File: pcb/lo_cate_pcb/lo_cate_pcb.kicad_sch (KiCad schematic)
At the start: 42 parts, among them J1 Conn_01x07_Pin, J2 690-005-299-043, SW1 MICRO_RESET, SW2 MICRO_ON, SW3 BUTTON1, SW4 BUTTON2, SW5 BUTTON3, U1 STM32F401RETx, U2 BMI323, U3 150141M173100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

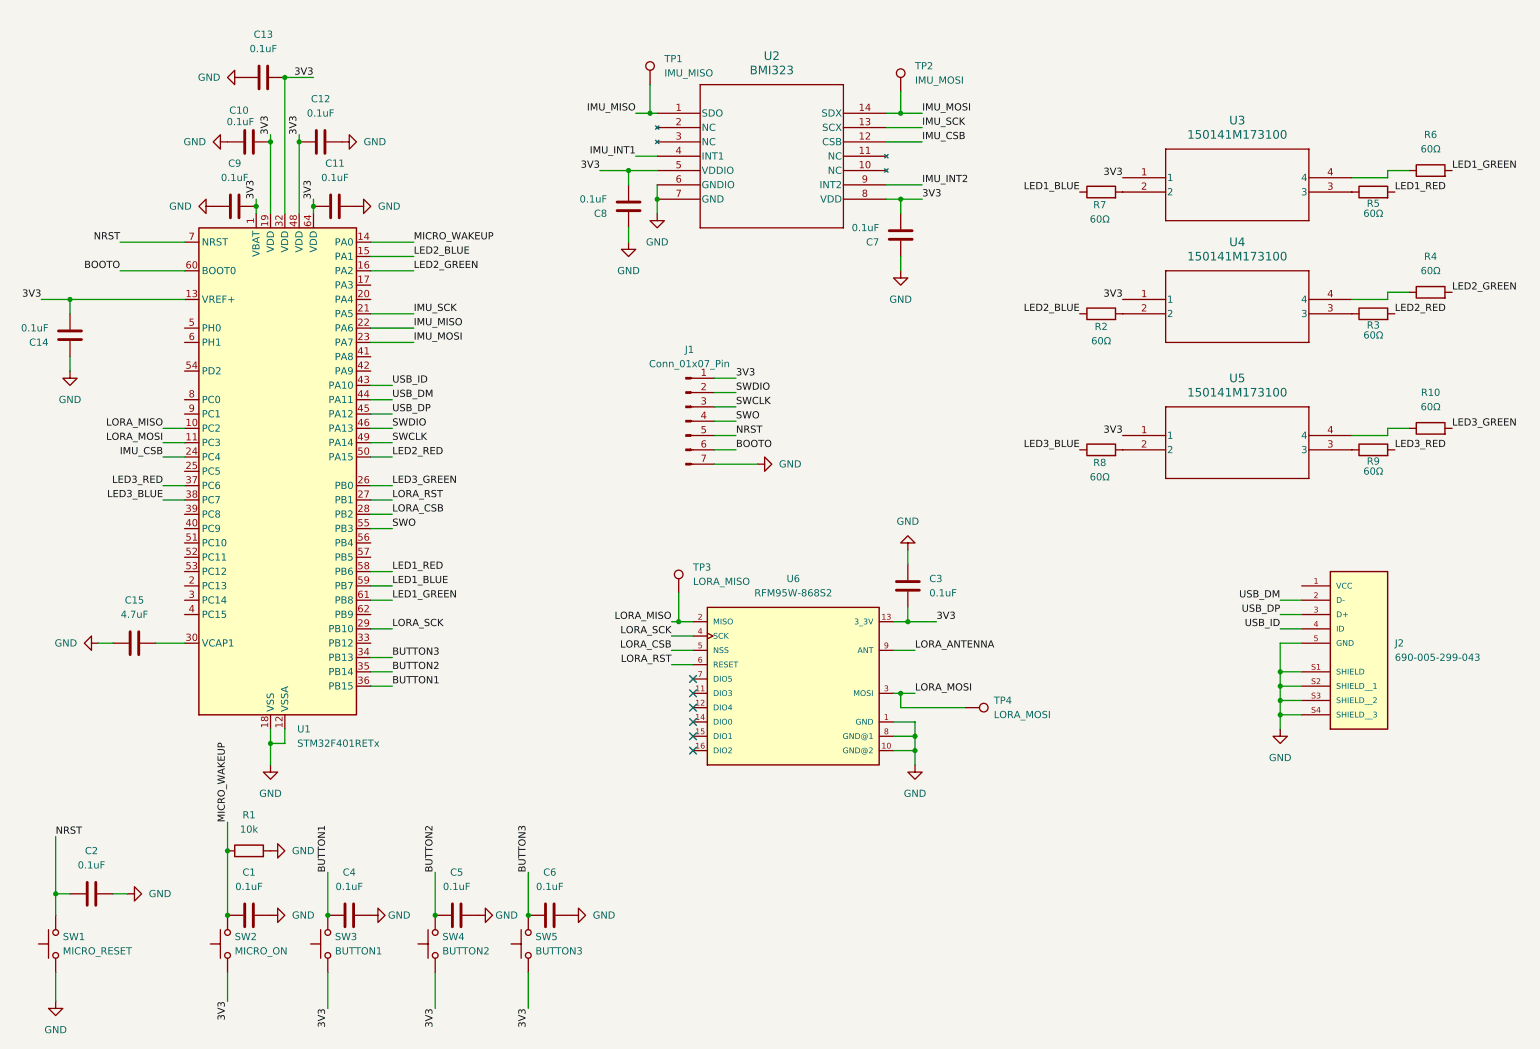
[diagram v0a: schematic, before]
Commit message: Started the PCB Layout
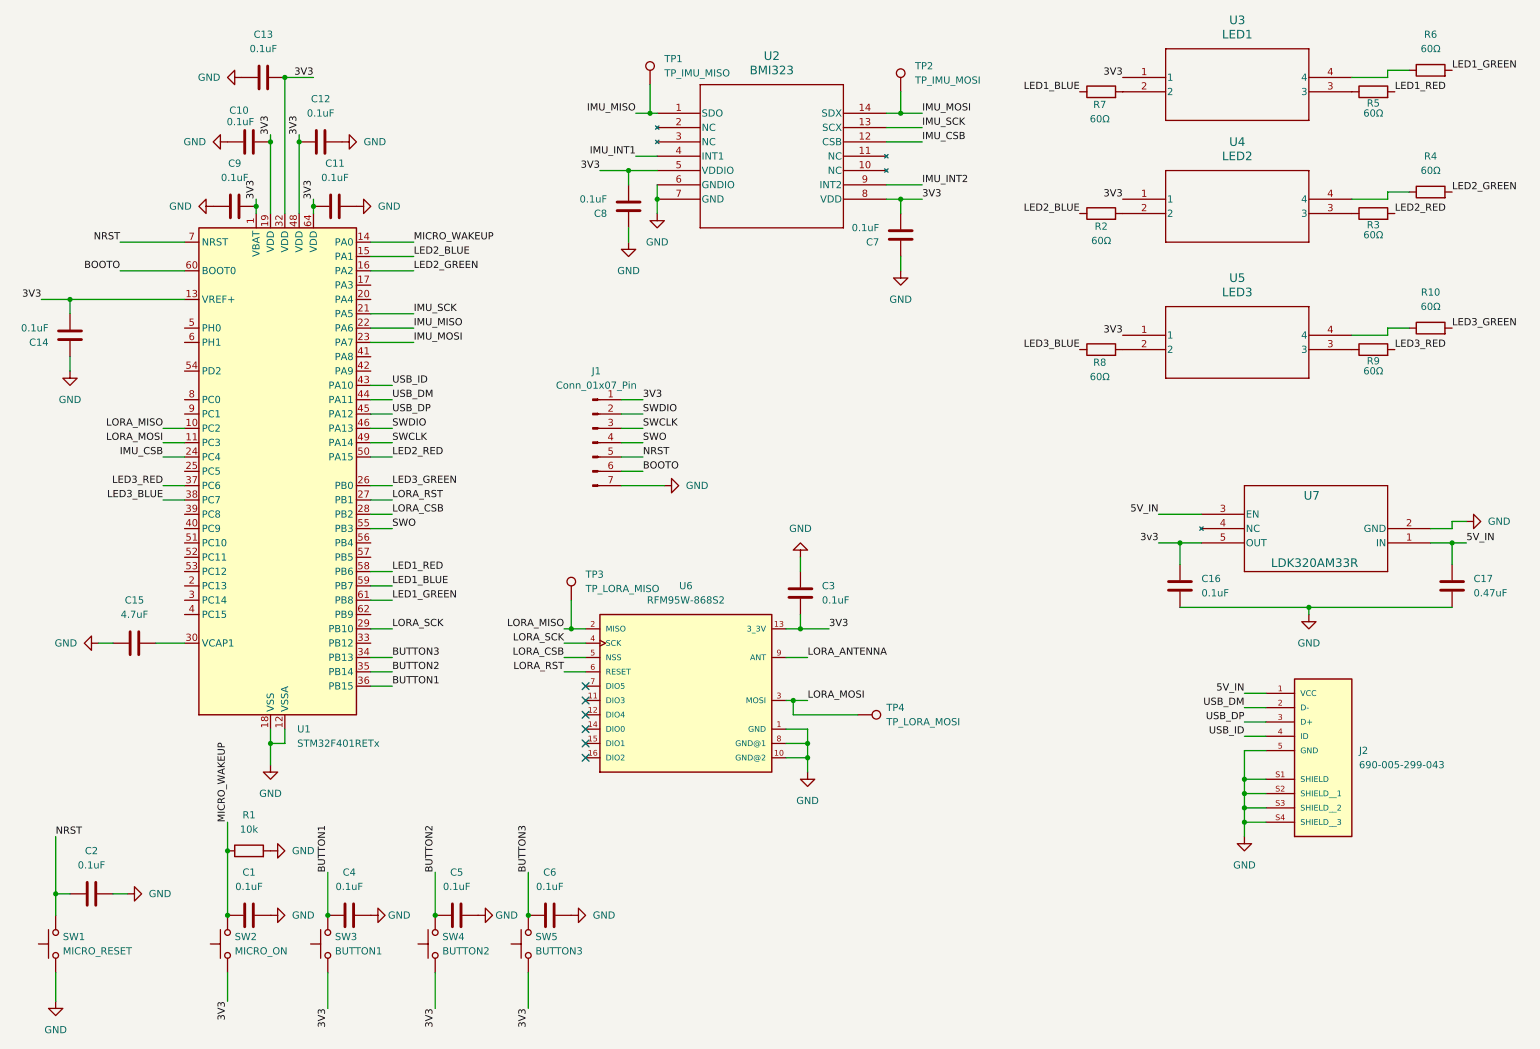
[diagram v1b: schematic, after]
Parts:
- added C16: 0.1uF, Capacitor_SMD:C_0805_2012Metric_Pad1.18x1.45mm_HandSolder, symbol Device:C
- added C17: 0.47uF, Capacitor_SMD:C_0805_2012Metric_Pad1.18x1.45mm_HandSolder, symbol Device:C
- added U7: LDK320AM33R, footprints:SOT23-5L_STM-M, symbol 2024-06-23_08-34-14:LDK320AM33R
- C1, C10, C11, C12, C13, C14, C15, C2, C3, C4, C5, C6, C7, C8, C9: footprint Capacitor_SMD:C_1206_3216Metric_Pad1.33x1.80mm_HandSolder -> Capacitor_SMD:C_0805_2012Metric_Pad1.18x1.45mm_HandSolder
- J2: footprint 690-005-299-043:EDAC_690-005-299-043 -> footprints:EDAC_690-005-299-043
- R1, R10, R2, R3, R4, R5, R6, R7, R8, R9: footprint Resistor_SMD:R_1206_3216Metric_Pad1.30x1.75mm_HandSolder -> Resistor_SMD:R_0805_2012Metric_Pad1.20x1.40mm_HandSolder
- SW1: footprint Resistor_SMD:R_1206_3216Metric_Pad1.30x1.75mm_HandSolder -> Button_Switch_SMD:SW_SPST_PTS647_Sx38
- TP1: value IMU_MISO -> TP_IMU_MISO; footprint (none) -> TestPoint:TestPoint_Pad_D2.0mm
- TP2: value IMU_MOSI -> TP_IMU_MOSI; footprint (none) -> TestPoint:TestPoint_Pad_D2.0mm
- TP3: value LORA_MISO -> TP_LORA_MISO; footprint (none) -> TestPoint:TestPoint_Pad_D2.0mm
- TP4: value LORA_MOSI -> TP_LORA_MOSI; footprint (none) -> TestPoint:TestPoint_Pad_D2.0mm
- U3: value 150141M173100 -> LED1
- U4: value 150141M173100 -> LED2
- U5: value 150141M173100 -> LED3
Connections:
- net GND: now also C16.2, C17.2, U7.2 (GND)
- net 5V_IN: now reaches J2.1 (VCC)
- net 5V_IN: now also C17.1, U7.1 (IN), U7.3 (EN)
- new net 3v3: C16.1, U7.5 (OUT)
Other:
- moved on the sheet: C3, J1, J2, R10, R2, R3, R4, R5, R6, R7, R8, R9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

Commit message: Added smt connector
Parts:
- added H1, H3, H4: MountingHole, MountingHole:MountingHole_3.2mm_M3, symbol Mechanical:MountingHole
- added J3: U.FL-R-SMT-110, footprints:CONN1_UFL-R_HIR, symbol 2024-06-24_09-28-13:U.FL-R-SMT-110
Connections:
- net LORA_ANTENNA: no longer names the net of U6.9 (ANT)
- net LORA_ANTENNA: now also J3.1
